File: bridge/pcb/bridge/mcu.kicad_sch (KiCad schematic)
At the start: 25 parts, among them J5 Conn_01x04, J6 Conn_01x02, J7 Conn_01x03, J8 Conn_01x02, J9 MCU_Test_Point, U1 L293, U4 ATmega328P-P, U5 L7805, U6 MCP4901

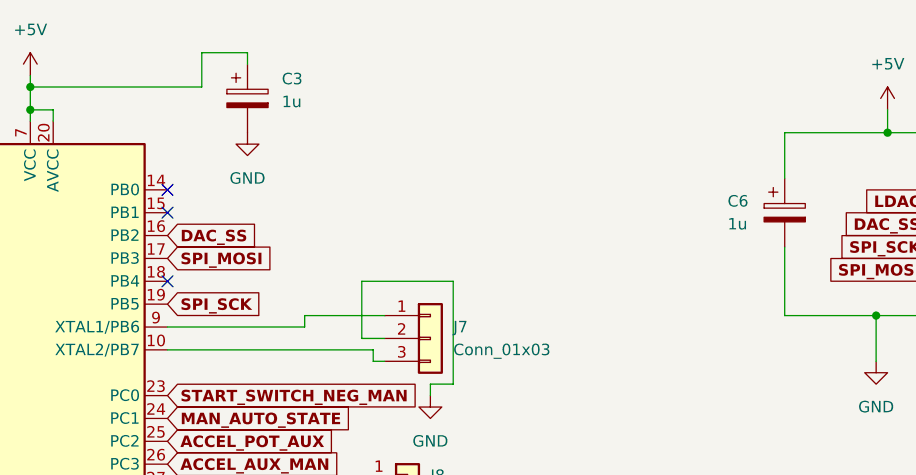
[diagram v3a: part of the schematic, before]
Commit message: Added connector for manual mode forward and reverse signals
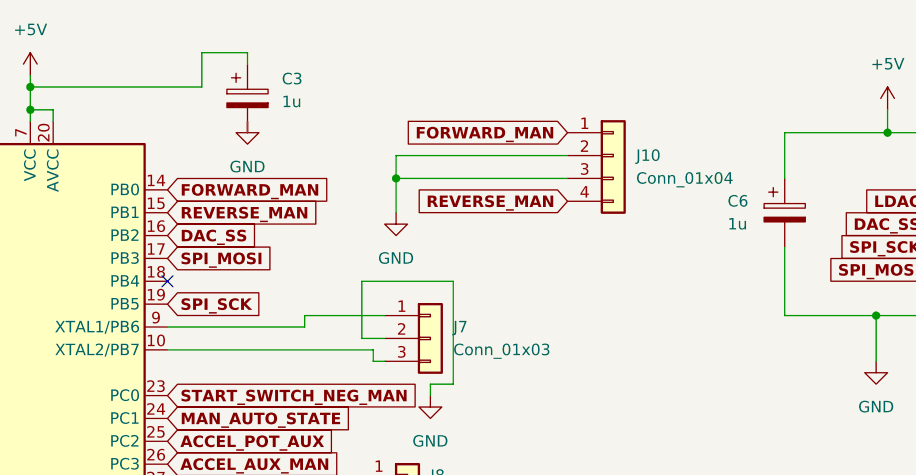
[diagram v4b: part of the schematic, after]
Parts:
- added J10: Conn_01x04, symbol Connector_Generic:Conn_01x04
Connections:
- net GND: now also J10.2 (Pin_2), J10.3 (Pin_3)
- net FORWARD_MAN: now reaches U4.14 (PB0)
- net FORWARD_MAN: now also J10.1 (Pin_1)
- net REVERSE_MAN: now reaches U4.15 (PB1)
- net REVERSE_MAN: now also J10.4 (Pin_4)
- no-connect marks 6 -> 4
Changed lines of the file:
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@@
   (junction (at 140.97 26.67) (diameter 0) (color 0 0 0 0)
   )
+  (junction (at 86.36 31.75) (diameter 0) (color 0 0 0 0)
+  )
   (junction (at 104.14 120.65) (diameter 0) (color 0 0 0 0)
   )
@@
   )
   (no_connect (at 60.96 66.04))
-  (no_connect (at 60.96 33.02))
   (no_connect (at 60.96 43.18))
-  (no_connect (at 60.96 35.56))
   (no_connect (at 60.96 68.58))
   (no_connect (at 30.48 33.02))
@@
     (stroke (width 0) (type default))
   )
+  (wire (pts (xy 86.36 31.75) (xy 86.36 35.56))
+    (stroke (width 0) (type default))
+  )
   (wire (pts (xy 82.55 49.53) (xy 82.55 43.18))
     (stroke (width 0) (type default))
@@
     (stroke (width 0) (type default))
   )
+  (wire (pts (xy 105.41 29.21) (xy 86.36 29.21))
+    (stroke (width 0) (type default))
+  )
   (wire (pts (xy 245.11 68.58) (xy 245.11 71.12))
     (stroke (width 0) (type default))
@@
     (stroke (width 0) (type default))
   )
+  (wire (pts (xy 105.41 31.75) (xy 86.36 31.75))
+    (stroke (width 0) (type default))
+  )
   (wire (pts (xy 139.7 52.07) (xy 139.7 46.99))
     (stroke (width 0) (type default))
@@
     (stroke (width 0) (type default))
   )
+  (wire (pts (xy 86.36 29.21) (xy 86.36 31.75))
+    (stroke (width 0) (type default))
+  )
   (wire (pts (xy 45.72 24.13) (xy 45.72 25.4))
     (stroke (width 0) (type default))
@@
   )
   (wire (pts (xy 48.26 25.4) (xy 48.26 24.13))
+    (stroke (width 0) (type default))
+  )
+  (wire (pts (xy 69.85 25.4) (xy 69.85 26.67))
     (stroke (width 0) (type default))
   )
@@
     )
   )
+  (global_label "FORWARD_MAN" (shape input) (at 60.96 33.02 0) (fields_autoplaced)
+    (effects (font (size 1.27 1.27) (thickness 0.254) bold) (justify left))
+    (property "Intersheetrefs" "${INTERSHEET_REFS}" (at 78.0284 33.02 0)
+      (effects (font (size 1.27 1.27)) (justify left) hide)
+    )
+  )
   (global_label "MCU_TURF" (shape input) (at 161.29 105.41 180) (fields_autoplaced)
     (effects (font (size 1.27 1.27) (thickness 0.254) bold) (justify right))
@@
     )
   )
+  (global_label "REVERSE_MAN" (shape input) (at 105.41 34.29 180) (fields_autoplaced)
+    (effects (font (size 1.27 1.27) (thickness 0.254) bold) (justify right))
+    (property "Intersheetrefs" "${INTERSHEET_REFS}" (at 88.8256 34.29 0)
+      (effects (font (size 1.27 1.27)) (justify right) hide)
+    )
+  )
   (global_label "REVERSE_SWITCH" (shape input) (at 245.11 125.73 90) (fields_autoplaced)
     (effects (font (size 1.27 1.27) bold) (justify left))
@@
     (property "Intersheetrefs" "${INTERSHEET_REFS}" (at 188.9417 36.83 0)
       (effects (font (size 1.27 1.27)) (justify left) hide)
+    )
+  )
+  (global_label "REVERSE_MAN" (shape input) (at 60.96 35.56 0) (fields_autoplaced)
+    (effects (font (size 1.27 1.27) (thickness 0.254) bold) (justify left))
+    (property "Intersheetrefs" "${INTERSHEET_REFS}" (at 77.5444 35.56 0)
+      (effects (font (size 1.27 1.27)) (justify left) hide)
+    )
+  )
+  (global_label "FORWARD_MAN" (shape input) (at 105.41 26.67 180) (fields_autoplaced)
+    (effects (font (size 1.27 1.27) (thickness 0.254) bold) (justify right))
+    (property "Intersheetrefs" "${INTERSHEET_REFS}" (at 88.3416 26.67 0)
+      (effects (font (size 1.27 1.27)) (justify right) hide)
     )
   )
@@
     )
   )
-  (symbol (lib_id "power:GND") (at 69.85 26.67 0) (unit 1)
-    (in_bom yes) (on_board yes) (dnp no) (fields_autoplaced)
-    (property "Reference" "#PWR036" (at 69.85 33.02 0)
-      (effects (font (size 1.27 1.27)) hide)
-    )
-    (property "Value" "GND" (at 69.85 31.75 0)
-      (effects (font (size 1.27 1.27)))
-    )
-    (property "Footprint" "" (at 69.85 26.67 0)
-      (effects (font (size 1.27 1.27)) hide)
-    )
-    (property "Datasheet" "" (at 69.85 26.67 0)
+  (symbol (lib_id "power:GND") (at 69.85 25.4 0) (unit 1)
+    (in_bom yes) (on_board yes) (dnp no) (fields_autoplaced)
+    (property "Reference" "#PWR036" (at 69.85 31.75 0)
+      (effects (font (size 1.27 1.27)) hide)
+    )
+    (property "Value" "GND" (at 69.85 30.48 0)
+      (effects (font (size 1.27 1.27)))
+    )
+    (property "Footprint" "" (at 69.85 25.4 0)
+      (effects (font (size 1.27 1.27)) hide)
+    )
+    (property "Datasheet" "" (at 69.85 25.4 0)
       (effects (font (size 1.27 1.27)) hide)
     )
@@
         (path "/40a0f45e-7290-47b9-8da3-09f7dfbfbbd7/00f451ee-7b68-4840-8f31-2bfc247688fa"
           (reference "#PWR036") (unit 1)
+        )
+      )
+    )
+  )
+  (symbol (lib_id "Connector_Generic:Conn_01x04") (at 110.49 29.21 0) (unit 1)
+    (in_bom yes) (on_board yes) (dnp no) (fields_autoplaced)
+    (property "Reference" "J10" (at 113.03 29.21 0)
+      (effects (font (size 1.27 1.27)) (justify left))
+    )
+    (property "Value" "Conn_01x04" (at 113.03 31.75 0)
+      (effects (font (size 1.27 1.27)) (justify left))
+    )
+    (property "Footprint" "" (at 110.49 29.21 0)
+      (effects (font (size 1.27 1.27)) hide)
+    )
+    (property "Datasheet" "~" (at 110.49 29.21 0)
+      (effects (font (size 1.27 1.27)) hide)
+    )
+    (pin "2")
+    (pin "1")
+    (pin "4")
+    (pin "3")
+    (instances
+      (project "bridge"
+        (path "/40a0f45e-7290-47b9-8da3-09f7dfbfbbd7/00f451ee-7b68-4840-8f31-2bfc247688fa"
+          (reference "J10") (unit 1)
         )
       )
@@
         )
       )
+    )
+  )
+  (symbol (lib_id "power:GND") (at 86.36 35.56 0) (unit 1)
+    (in_bom yes) (on_board yes) (dnp no) (fields_autoplaced)
+    (property "Reference" "#PWR029" (at 86.36 41.91 0)
+      (effects (font (size 1.27 1.27)) hide)
+    )
+    (property "Value" "GND" (at 86.36 40.64 0)
+      (effects (font (size 1.27 1.27)))
+    )
+    (property "Footprint" "" (at 86.36 35.56 0)
+      (effects (font (size 1.27 1.27)) hide)
+    )
+    (property "Datasheet" "" (at 86.36 35.56 0)
+      (effects (font (size 1.27 1.27)) hide)
+    )
+    (pin "1")
+    (instances
+      (project "bridge"
+        (path "/40a0f45e-7290-47b9-8da3-09f7dfbfbbd7/00f451ee-7b68-4840-8f31-2bfc247688fa"
+          (reference "#PWR029") (unit 1)
+        )
+      )

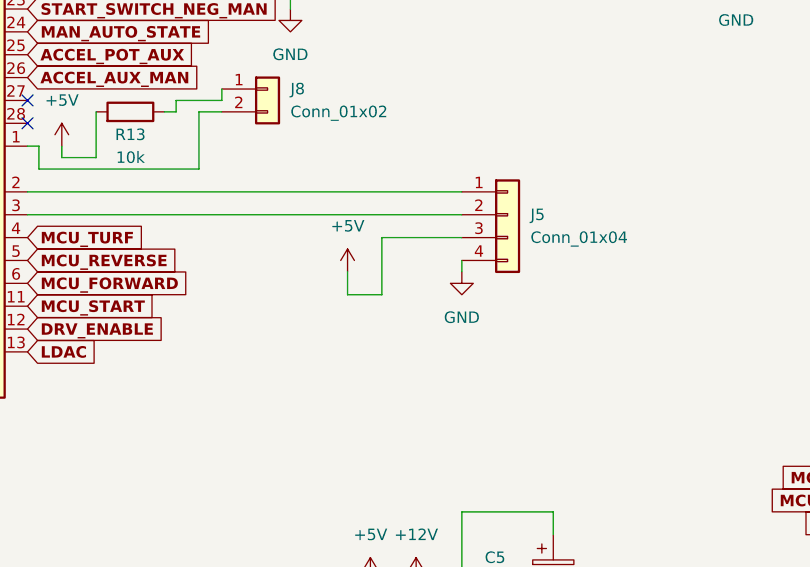
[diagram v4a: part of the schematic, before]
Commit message: Reversed 5V and GND on serial connector symbol
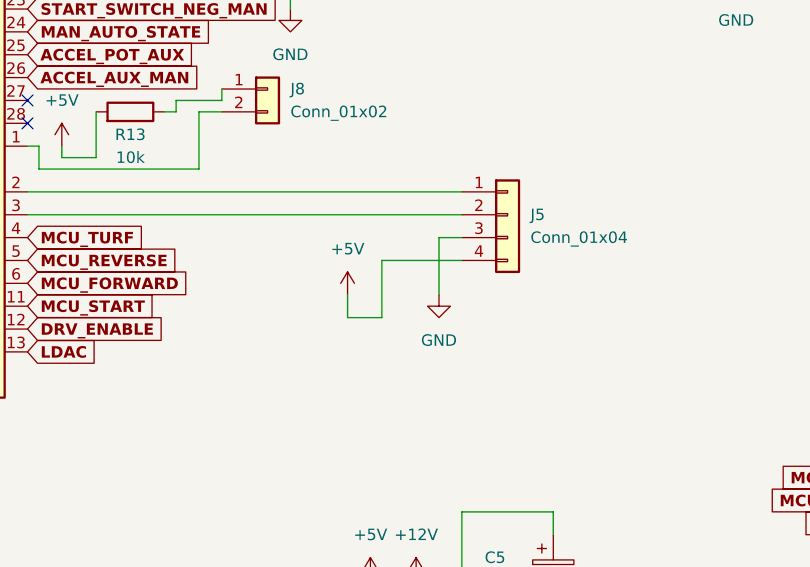
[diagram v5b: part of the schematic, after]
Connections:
- net +5V: now also J5.4 (Pin_4); no longer J5.3 (Pin_3)
- net GND: now also J5.3 (Pin_3); no longer J5.4 (Pin_4)
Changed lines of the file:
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@@
   (no_connect (at 60.96 68.58))
   (no_connect (at 30.48 33.02))
-  (wire (pts (xy 100.33 81.28) (xy 109.22 81.28))
-    (stroke (width 0) (type default))
-  )
   (wire (pts (xy 232.41 60.96) (xy 234.95 60.96))
     (stroke (width 0) (type default))
@@
     (stroke (width 0) (type default))
   )
-  (wire (pts (xy 109.22 83.82) (xy 109.22 85.09))
-    (stroke (width 0) (type default))
-  )
-  (wire (pts (xy 96.52 87.63) (xy 96.52 85.09))
-    (stroke (width 0) (type default))
-  )
   (wire (pts (xy 245.11 71.12) (xy 245.11 72.39))
     (stroke (width 0) (type default))
@@
     (stroke (width 0) (type default))
   )
+  (wire (pts (xy 96.52 90.17) (xy 96.52 87.63))
+    (stroke (width 0) (type default))
+  )
   (wire (pts (xy 139.7 46.99) (xy 156.21 46.99))
     (stroke (width 0) (type default))
   )
+  (wire (pts (xy 109.22 81.28) (xy 106.68 81.28))
+    (stroke (width 0) (type default))
+  )
   (wire (pts (xy 234.95 60.96) (xy 237.49 60.96))
     (stroke (width 0) (type default))
@@
     (stroke (width 0) (type default))
   )
-  (wire (pts (xy 100.33 87.63) (xy 96.52 87.63))
-    (stroke (width 0) (type default))
-  )
   (wire (pts (xy 233.68 137.16) (xy 233.68 139.7))
     (stroke (width 0) (type default))
   )
+  (wire (pts (xy 100.33 90.17) (xy 96.52 90.17))
+    (stroke (width 0) (type default))
+  )
   (wire (pts (xy 99.06 119.38) (xy 99.06 121.92))
     (stroke (width 0) (type default))
@@
     (stroke (width 0) (type default))
   )
+  (wire (pts (xy 106.68 81.28) (xy 106.68 87.63))
+    (stroke (width 0) (type default))
+  )
   (wire (pts (xy 90.17 54.61) (xy 90.17 55.88))
     (stroke (width 0) (type default))
@@
     (stroke (width 0) (type default))
   )
-  (wire (pts (xy 100.33 81.28) (xy 100.33 87.63))
-    (stroke (width 0) (type default))
-  )
   (wire (pts (xy 176.53 113.03) (xy 176.53 114.3))
     (stroke (width 0) (type default))
@@
     (stroke (width 0) (type default))
   )
+  (wire (pts (xy 100.33 83.82) (xy 109.22 83.82))
+    (stroke (width 0) (type default))
+  )
   (wire (pts (xy 39.37 127) (xy 43.18 127))
+    (stroke (width 0) (type default))
+  )
+  (wire (pts (xy 100.33 83.82) (xy 100.33 90.17))
     (stroke (width 0) (type default))
   )
@@
     )
   )
+  (symbol (lib_id "power:GND") (at 106.68 87.63 0) (unit 1)
+    (in_bom yes) (on_board yes) (dnp no) (fields_autoplaced)
+    (property "Reference" "#PWR032" (at 106.68 93.98 0)
+      (effects (font (size 1.27 1.27)) hide)
+    )
+    (property "Value" "GND" (at 106.68 92.71 0)
+      (effects (font (size 1.27 1.27)))
+    )
+    (property "Footprint" "" (at 106.68 87.63 0)
+      (effects (font (size 1.27 1.27)) hide)
+    )
+    (property "Datasheet" "" (at 106.68 87.63 0)
+      (effects (font (size 1.27 1.27)) hide)
+    )
+    (pin "1")
+    (instances
+      (project "bridge"
+        (path "/40a0f45e-7290-47b9-8da3-09f7dfbfbbd7/00f451ee-7b68-4840-8f31-2bfc247688fa"
+          (reference "#PWR032") (unit 1)
+        )
+      )
+    )
+  )
   (symbol (lib_id "power:GND") (at 45.72 102.87 0) (unit 1)
     (in_bom yes) (on_board yes) (dnp no) (fields_autoplaced)
@@
         (path "/40a0f45e-7290-47b9-8da3-09f7dfbfbbd7/00f451ee-7b68-4840-8f31-2bfc247688fa"
           (reference "J5") (unit 1)
-        )
-      )
-    )
-  )
-  (symbol (lib_id "power:+5V") (at 96.52 85.09 0) (mirror y) (unit 1)
-    (in_bom yes) (on_board yes) (dnp no) (fields_autoplaced)
-    (property "Reference" "#PWR034" (at 96.52 88.9 0)
-      (effects (font (size 1.27 1.27)) hide)
-    )
-    (property "Value" "+5V" (at 96.52 80.01 0)
-      (effects (font (size 1.27 1.27)))
-    )
-    (property "Footprint" "" (at 96.52 85.09 0)
-      (effects (font (size 1.27 1.27)) hide)
-    )
-    (property "Datasheet" "" (at 96.52 85.09 0)
-      (effects (font (size 1.27 1.27)) hide)
-    )
-    (pin "1")
-    (instances
-      (project "bridge"
-        (path "/40a0f45e-7290-47b9-8da3-09f7dfbfbbd7/00f451ee-7b68-4840-8f31-2bfc247688fa"
-          (reference "#PWR034") (unit 1)
         )
       )
@@
     )
   )
+  (symbol (lib_id "power:+5V") (at 96.52 87.63 0) (mirror y) (unit 1)
+    (in_bom yes) (on_board yes) (dnp no) (fields_autoplaced)
+    (property "Reference" "#PWR034" (at 96.52 91.44 0)
+      (effects (font (size 1.27 1.27)) hide)
+    )
+    (property "Value" "+5V" (at 96.52 82.55 0)
+      (effects (font (size 1.27 1.27)))
+    )
+    (property "Footprint" "" (at 96.52 87.63 0)
+      (effects (font (size 1.27 1.27)) hide)
+    )
+    (property "Datasheet" "" (at 96.52 87.63 0)
+      (effects (font (size 1.27 1.27)) hide)
+    )
+    (pin "1")
+    (instances
+      (project "bridge"
+        (path "/40a0f45e-7290-47b9-8da3-09f7dfbfbbd7/00f451ee-7b68-4840-8f31-2bfc247688fa"
+          (reference "#PWR034") (unit 1)
+        )
+      )
+    )
+  )
   (symbol (lib_id "power:GND") (at 119.38 123.19 0) (unit 1)
     (in_bom yes) (on_board yes) (dnp no) (fields_autoplaced)
@@
         )
       )
-    )
-  )
-  (symbol (lib_id "power:GND") (at 109.22 85.09 0) (unit 1)
-    (in_bom yes) (on_board yes) (dnp no) (fields_autoplaced)
-    (property "Reference" "#PWR032" (at 109.22 91.44 0)
-      (effects (font (size 1.27 1.27)) hide)
-    )
-    (property "Value" "GND" (at 109.22 90.17 0)
-      (effects (font (size 1.27 1.27)))
-    )
-    (property "Footprint" "" (at 109.22 85.09 0)
-      (effects (font (size 1.27 1.27)) hide)
-    )
-    (property "Datasheet" "" (at 109.22 85.09 0)
-      (effects (font (size 1.27 1.27)) hide)
-    )
-    (pin "1")
-    (instances
-      (project "bridge"
-        (path "/40a0f45e-7290-47b9-8da3-09f7dfbfbbd7/00f451ee-7b68-4840-8f31-2bfc247688fa"
-          (reference "#PWR032") (unit 1)
-        )
-      )

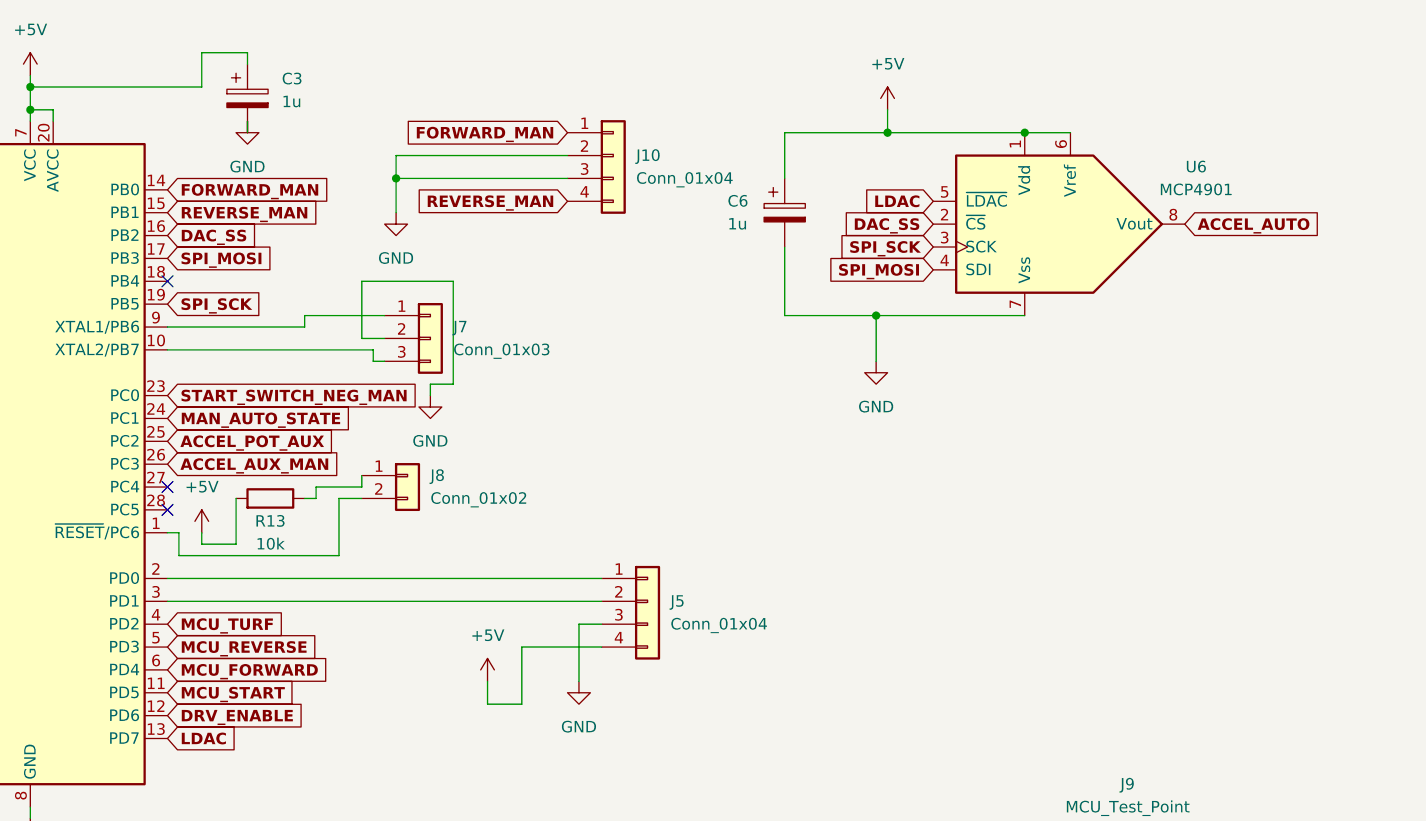
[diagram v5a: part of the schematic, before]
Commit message: Fixed schematic for manual forward, reverse, and turf switches
Seperated forward and reverse

Added turf

Changed schematic to use switch symbol instead of connector generic
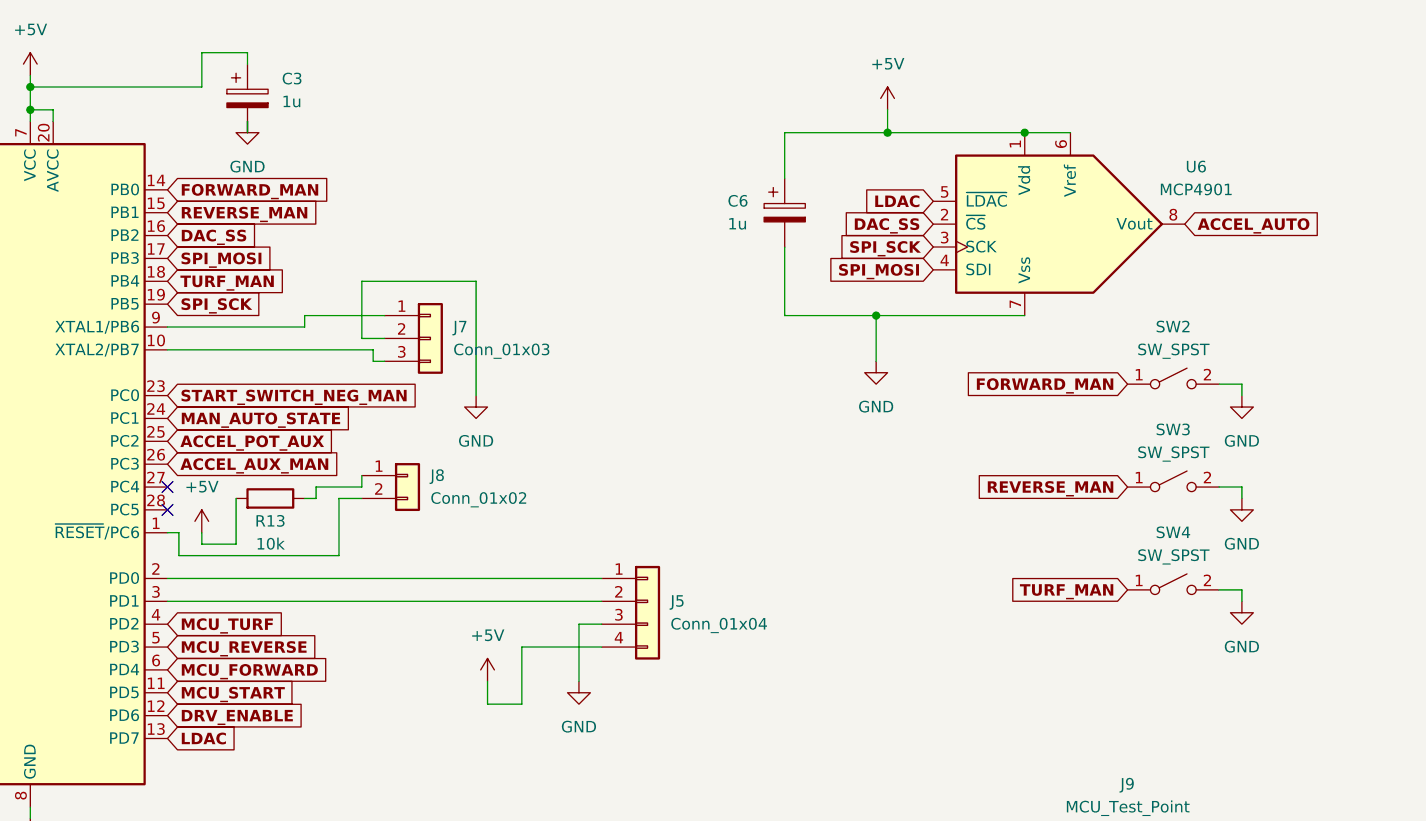
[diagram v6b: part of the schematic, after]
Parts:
- removed J10: Conn_01x04, symbol Connector_Generic:Conn_01x04
- added SW2, SW3, SW4: SW_SPST, symbol Switch:SW_SPST
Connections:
- net FORWARD_MAN: now also SW2.1 (A)
- net GND: now also SW2.2 (B), SW3.2 (B), SW4.2 (B)
- net REVERSE_MAN: now also SW3.1 (A)
- net TURF_MAN: now reaches U4.18 (PB4)
- net TURF_MAN: now also SW4.1 (A)
- no-connect marks 4 -> 3

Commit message: Assigned footprints and added new components to PCB
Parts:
- SW2, SW3, SW4: footprint (none) -> Connector_PinHeader_2.54mm:PinHeader_1x02_P2.54mm_Vertical
- U6: footprint (none) -> Package_DIP:DIP-8_W7.62mm
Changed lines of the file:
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@@
       (effects (font (size 1.27 1.27)))
     )
-    (property "Footprint" "" (at 172.72 54.61 0)
+    (property "Footprint" "Connector_PinHeader_2.54mm:PinHeader_1x02_P2.54mm_Vertical" (at 172.72 54.61 0)
       (effects (font (size 1.27 1.27)) hide)
     )
@@
       (effects (font (size 1.27 1.27)))
     )
-    (property "Footprint" "" (at 181.61 39.37 0)
+    (property "Footprint" "Package_DIP:DIP-8_W7.62mm" (at 181.61 39.37 0)
       (effects (font (size 1.27 1.27)) hide)
     )
@@
       (effects (font (size 1.27 1.27)))
     )
-    (property "Footprint" "" (at 172.72 77.47 0)
+    (property "Footprint" "Connector_PinHeader_2.54mm:PinHeader_1x02_P2.54mm_Vertical" (at 172.72 77.47 0)
       (effects (font (size 1.27 1.27)) hide)
     )
@@
       (effects (font (size 1.27 1.27)))
     )
-    (property "Footprint" "" (at 172.72 66.04 0)
-      (effects (font (size 1.27 1.27)) hide)
-    )
+    (property "Footprint" "Connector_PinHeader_2.54mm:PinHeader_1x02_P2.54mm_Vertical" (at 172.72 66.04 0)
+      (effects (font (size 1.27 1.27)) hide)
+    )
